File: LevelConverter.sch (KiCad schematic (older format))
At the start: 3 parts, among them U401 PI4ULS5V201TAEX

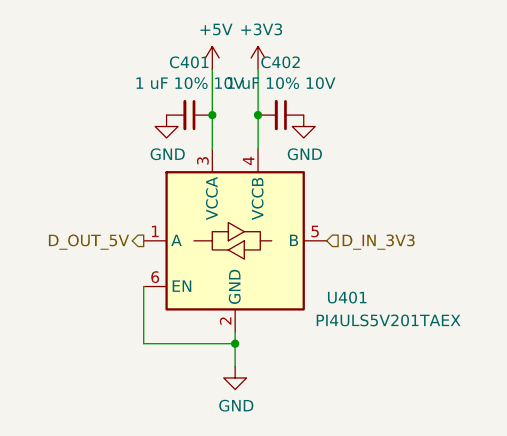
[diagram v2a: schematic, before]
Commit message: Fix design error in PI4ULS5V201TAEX. Reset and reassigned all annotations.
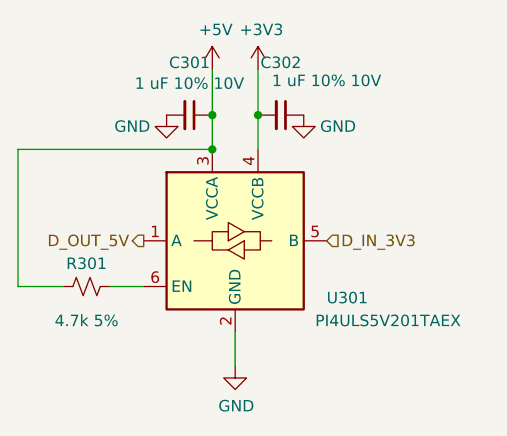
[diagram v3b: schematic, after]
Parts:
- added R301: 4.7k 5%, Resistor_SMD:R_0805_2012Metric_Pad1.20x1.40mm_HandSolder, symbol Device:R_Small_US
- renumbered C401 to C301, C402 to C302, U401 to U301
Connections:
- net +5V: now also R301.2
- net GND: no longer U301.6 (EN)
- new net: R301.1, U301.6 (EN)
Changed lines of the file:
@@
 $EndDescr
 $Comp
-L power:+5V #PWR0402
+L power:+5V #PWR0302
 U 1 1 61A863EC
 P 5500 3050
-F 0 "#PWR0402" H 5500 2900 50  0001 C CNN
+F 0 "#PWR0302" H 5500 2900 50  0001 C CNN
 F 1 "+5V" H 5515 3223 50  0000 C CNN
 F 2 "" H 5500 3050 50  0001 C CNN
@@
 $EndComp
 $Comp
-L power:+3V3 #PWR0404
+L power:+3V3 #PWR0304
 U 1 1 61A86F52
 P 5700 3050
-F 0 "#PWR0404" H 5700 2900 50  0001 C CNN
+F 0 "#PWR0304" H 5700 2900 50  0001 C CNN
 F 1 "+3V3" H 5715 3223 50  0000 C CNN
 F 2 "" H 5700 3050 50  0001 C CNN
@@
 $EndComp
 $Comp
-L power:GND #PWR0403
+L power:GND #PWR0303
 U 1 1 61A8764F
 P 5600 4350
-F 0 "#PWR0403" H 5600 4100 50  0001 C CNN
+F 0 "#PWR0303" H 5600 4100 50  0001 C CNN
 F 1 "GND" H 5605 4177 50  0000 C CNN
 F 2 "" H 5600 4350 50  0001 C CNN
@@
 $EndComp
 Wire Wire Line
-	5600 4200 5600 4250
-Wire Wire Line
-	5200 4000 5200 4250
-Wire Wire Line
-	5200 4250 5600 4250
-Connection ~ 5600 4250
-Wire Wire Line
-	5600 4250 5600 4350
-Wire Wire Line
 	5500 3050 5500 3250
 Wire Wire Line
 	5700 3050 5700 3250
 $Comp
-L Device:C_Small C401
+L Device:C_Small C301
 U 1 1 61A88161
 P 5400 3250
-F 0 "C401" V 5171 3250 50  0000 C CNN
+F 0 "C301" V 5171 3250 50  0000 C CNN
 F 1 "1 uF 10% 10V" V 5262 3250 50  0000 C CNN
 F 2 "Capacitor_SMD:C_0805_2012Metric_Pad1.18x1.45mm_HandSolder" H 5400 3250 50  0001 C CNN
@@
 	5500 3250 5500 3400
 $Comp
-L Device:C_Small C402
+L Device:C_Small C302
 U 1 1 61A889D1
 P 5800 3250
-F 0 "C402" V 5571 3250 50  0000 C CNN
-F 1 "1 uF 10% 10V" V 5662 3250 50  0000 C CNN
+F 0 "C302" V 5571 3250 50  0000 C CNN
+F 1 "1 uF 10% 10V" V 5650 3450 50  0000 C CNN
 F 2 "Capacitor_SMD:C_0805_2012Metric_Pad1.18x1.45mm_HandSolder" H 5800 3250 50  0001 C CNN
 F 3 "http://www.samsungsem.com/kr/support/product-search/mlcc/CL21B105KPFNNNE.jsp" H 5800 3250 50  0001 C CNN
@@
 	5700 3250 5700 3400
 $Comp
-L power:GND #PWR0405
+L power:GND #PWR0305
 U 1 1 61A88CCE
 P 5900 3250
-F 0 "#PWR0405" H 5900 3000 50  0001 C CNN
-F 1 "GND" H 5905 3077 50  0000 C CNN
+F 0 "#PWR0305" H 5900 3000 50  0001 C CNN
+F 1 "GND" H 6050 3200 50  0000 C CNN
 F 2 "" H 5900 3250 50  0001 C CNN
 F 3 "" H 5900 3250 50  0001 C CNN
@@
 $EndComp
 $Comp
-L TMPCB_R2:PI4ULS5V201TAEX U401
+L TMPCB_R2:PI4ULS5V201TAEX U301
 U 1 1 61A85D29
 P 5600 3800
-F 0 "U401" H 6000 3550 50  0000 L CNN
+F 0 "U301" H 6000 3550 50  0000 L CNN
 F 1 "PI4ULS5V201TAEX" H 5950 3450 50  0000 L CNN
 F 2 "Package_TO_SOT_SMD:SOT-23-6" H 5600 3350 50  0001 C CNN
@@
 $EndComp
 $Comp
-L power:GND #PWR0401
+L power:GND #PWR0301
 U 1 1 61A89F0F
 P 5300 3250
-F 0 "#PWR0401" H 5300 3000 50  0001 C CNN
-F 1 "GND" H 5305 3077 50  0000 C CNN
+F 0 "#PWR0301" H 5300 3000 50  0001 C CNN
+F 1 "GND" H 5150 3200 50  0000 C CNN
 F 2 "" H 5300 3250 50  0001 C CNN
 F 3 "" H 5300 3250 50  0001 C CNN
@@
 Text HLabel 6000 3800 2    50   Input ~ 0
 D_IN_3V3
+Wire Wire Line
+	5600 4200 5600 4350
+$Comp
+L Device:R_Small_US R301
+U 1 1 61D668D1
+P 4950 4000
+F 0 "R301" V 4850 4000 50  0000 C CNN
+F 1 "4.7k 5%" V 5100 4000 50  0000 C CNN
+F 2 "Resistor_SMD:R_0805_2012Metric_Pad1.20x1.40mm_HandSolder" H 4950 4000 50  0001 C CNN
+F 3 "~" H 4950 4000 50  0001 C CNN
+	1    4950 4000
+	0    1    1    0
+$EndComp
+Wire Wire Line
+	5200 4000 5050 4000
+Wire Wire Line
+	4850 4000 4650 4000
+Wire Wire Line
+	4650 4000 4650 3400
+Wire Wire Line
+	4650 3400 5500 3400
+Connection ~ 5500 3400
 $EndSCHEMATC
